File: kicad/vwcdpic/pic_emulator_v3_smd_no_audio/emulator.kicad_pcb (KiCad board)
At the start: 2 copper layers, 24.1 x 18.4 mm, 12 parts, among them P1 CONN_01X05, P2 CONN_01X02, U1 PIC12F629, U2 78L05

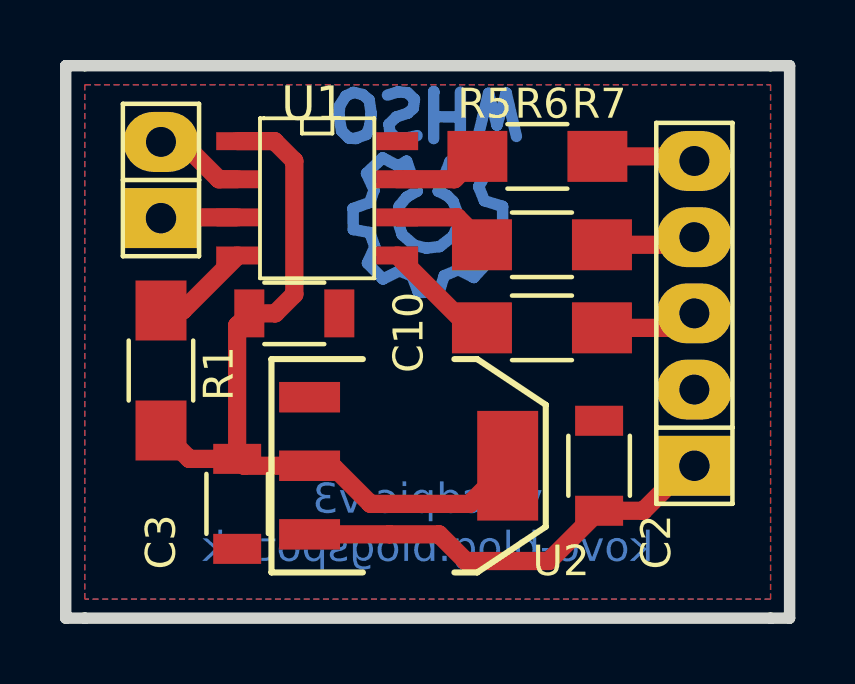
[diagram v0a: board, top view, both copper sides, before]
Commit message: update pcb with soic8 handsoldering module
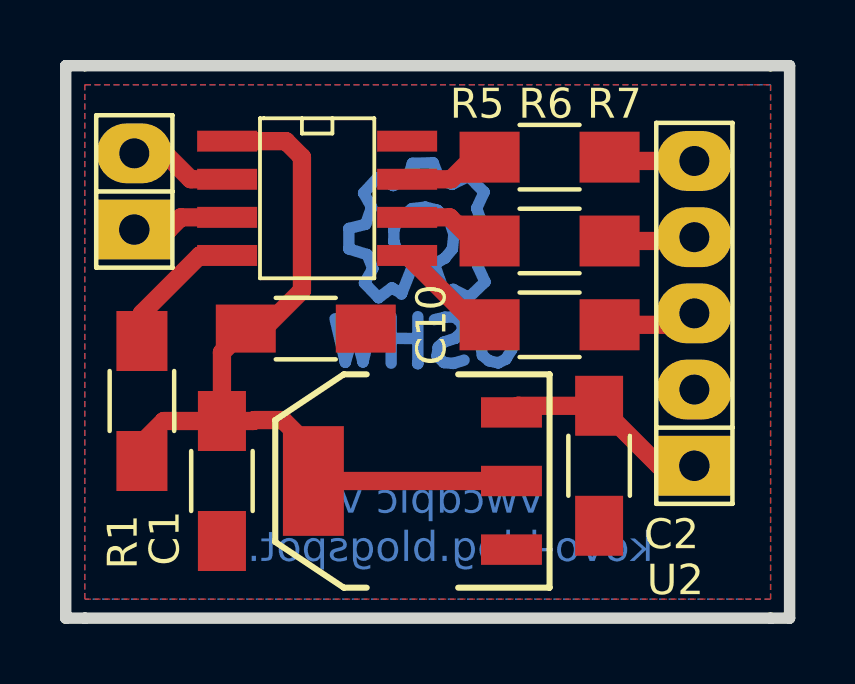
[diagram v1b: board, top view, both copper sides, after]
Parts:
- removed C3: 100n, Capacitors_SMD:C_1206
- added C1: 100n, Capacitors_SMD:C_1206_HandSoldering, F.Cu at (96.0, 58.3)
- C10, C2: footprint Capacitors_SMD:C_1206 -> Capacitors_SMD:C_1206_HandSoldering
- U1: footprint SMD_Packages:SOIC-8-W -> my_modules:SOIC-8-W_long_pads
- moved R1 1.20 mm to (93.3, 55.6)
- moved P2 0.97 mm to (93.1, 48.6)
- moved SYM 0.65 mm to (102.7, 50.2), turned to 180 degrees
- moved C10 0.64 mm to (98.8, 53.2)
- moved U2 0.52 mm to (102.4, 58.3), turned to 90 degrees
- moved R5 0.41 mm to (106.9, 47.5)
- moved R6 0.28 mm to (106.9, 50.3)
- moved R7 0.27 mm to (106.9, 53.1)
- turned C2 to 270 degrees
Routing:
- net POWER_CTL: track 14.6 -> 7.02 mm
- net +5V: track 26.5 -> 27.6 mm
- net Net-(R1-Pad1): track 3.86 -> 4.86 mm
- net Net-(P2-Pad2): track 3.06 -> 4.06 mm
- net Net-(P2-Pad1): track 2.55 -> 3.26 mm
- net DataOut: track 3.08 -> 3.67 mm

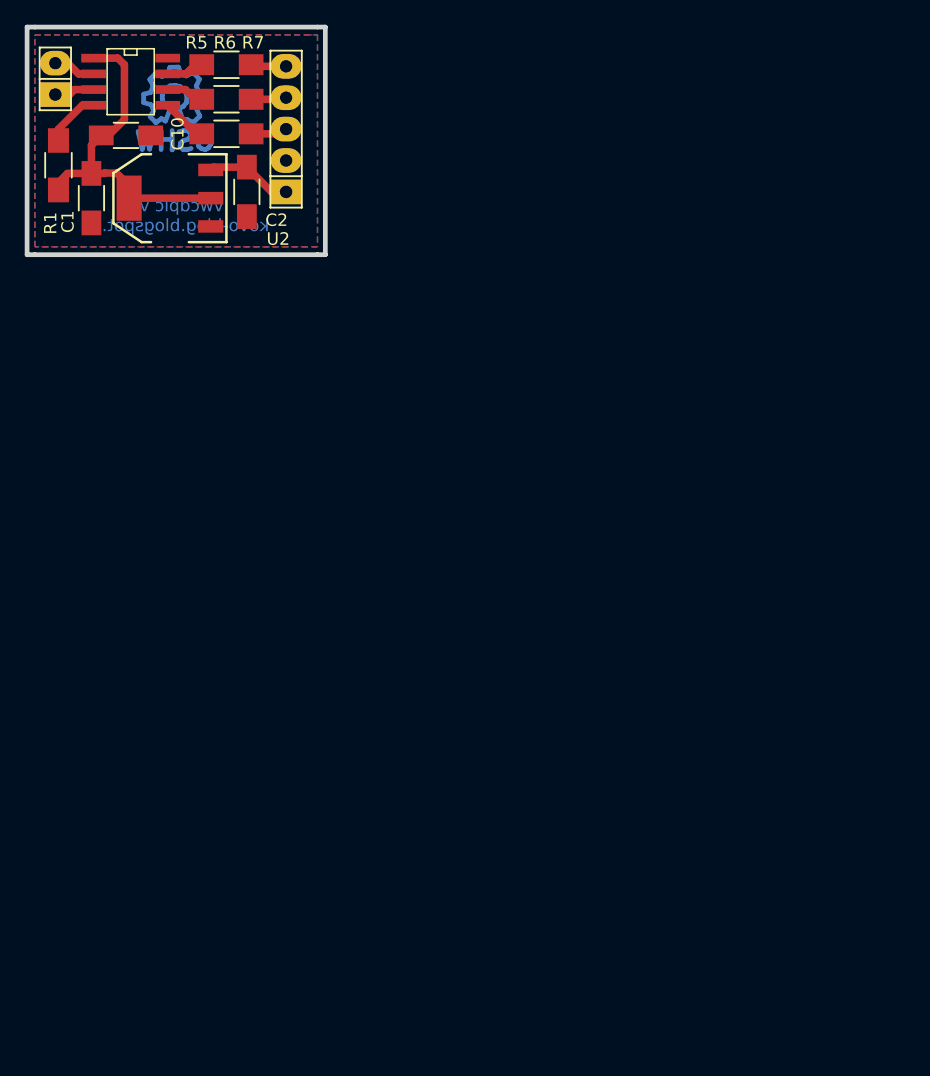
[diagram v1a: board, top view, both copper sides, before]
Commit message: vwcdpic v3 board/panelize
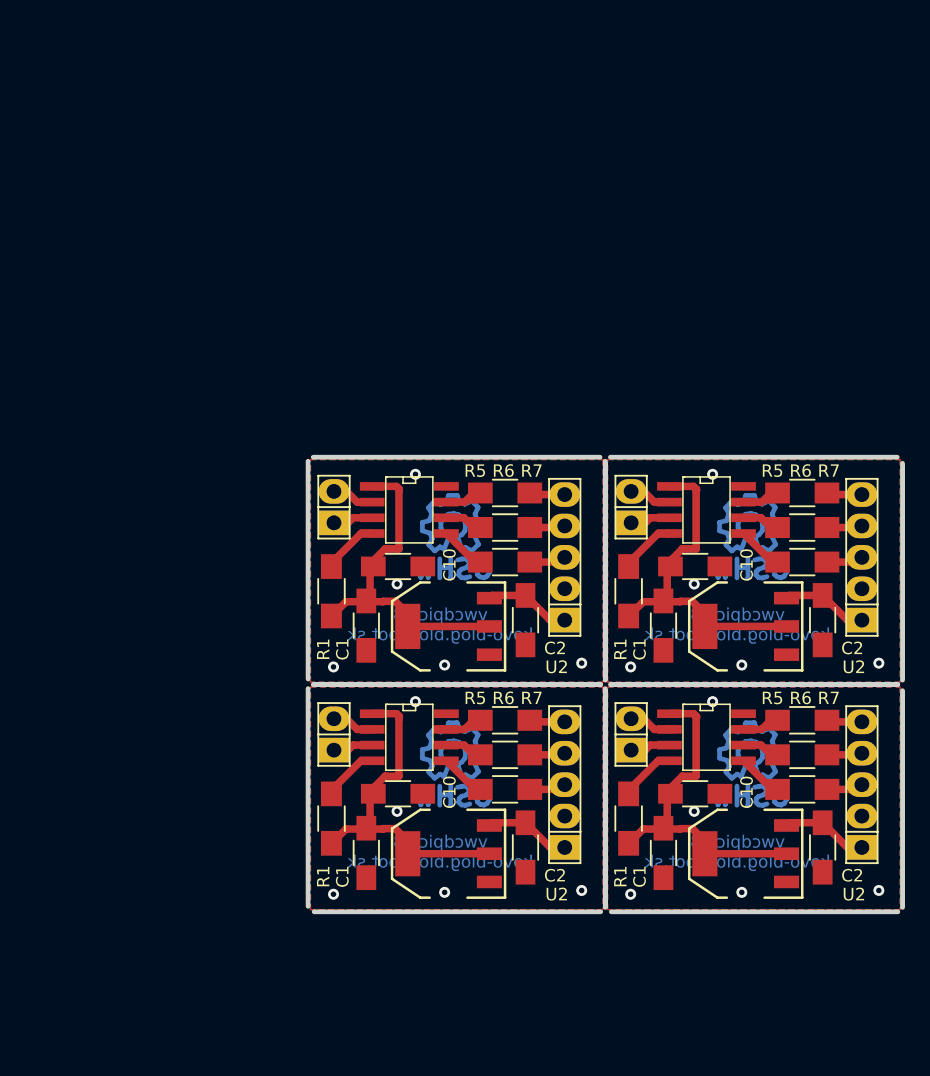
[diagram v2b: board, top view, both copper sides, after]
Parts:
- removed the C1 at (96.0, 58.3)
- removed the C10 at (98.8, 53.2)
- removed the C2 at (108.6, 57.8)
- removed the P1 at (111.8, 52.7)
- removed the P2 at (93.1, 48.6)
- removed the R1 at (93.3, 55.6)
- removed the R5 at (106.9, 47.5)
- removed the R6 at (106.9, 50.3)
- removed the R7 at (106.9, 53.1)
- removed the SYM at (102.7, 50.2)
- removed the U1 at (99.2, 48.9)
- removed the U2 at (102.4, 58.3)
- added C1: 100n, Capacitors_SMD:C_1206_HandSoldering, F.Cu at (118.2, 111.3)
- added C1: 100n, Capacitors_SMD:C_1206_HandSoldering, F.Cu at (118.2, 92.9)
- added C1: 100n, Capacitors_SMD:C_1206_HandSoldering, F.Cu at (142.3, 92.9)
- added C1: 100n, Capacitors_SMD:C_1206_HandSoldering, F.Cu at (142.3, 111.3)
- added C10: 100n, Capacitors_SMD:C_1206_HandSoldering, F.Cu at (120.8, 106.5)
- added C10: 100n, Capacitors_SMD:C_1206_HandSoldering, F.Cu at (120.8, 88.1)
- added C10: 100n, Capacitors_SMD:C_1206_HandSoldering, F.Cu at (144.9, 88.1)
- added C10: 100n, Capacitors_SMD:C_1206_HandSoldering, F.Cu at (144.9, 106.5)
- added C2: 100n, Capacitors_SMD:C_1206_HandSoldering, F.Cu at (131.1, 110.8)
- added C2: 100n, Capacitors_SMD:C_1206_HandSoldering, F.Cu at (131.1, 92.4)
- added C2: 100n, Capacitors_SMD:C_1206_HandSoldering, F.Cu at (155.2, 92.4)
- added C2: 100n, Capacitors_SMD:C_1206_HandSoldering, F.Cu at (155.2, 110.8)
- added P1: CONN_01X05, Pin_Headers:Pin_Header_Straight_1x05, F.Cu at (134.3, 105.7)
- added P1: CONN_01X05, Pin_Headers:Pin_Header_Straight_1x05, F.Cu at (134.3, 87.4)
- added P1: CONN_01X05, Pin_Headers:Pin_Header_Straight_1x05, F.Cu at (158.3, 87.4)
- added P1: CONN_01X05, Pin_Headers:Pin_Header_Straight_1x05, F.Cu at (158.3, 105.7)
- added P2: CONN_01X02, Pin_Headers:Pin_Header_Straight_1x02, F.Cu at (115.6, 101.7)
- added P2: CONN_01X02, Pin_Headers:Pin_Header_Straight_1x02, F.Cu at (115.6, 83.3)
- added P2: CONN_01X02, Pin_Headers:Pin_Header_Straight_1x02, F.Cu at (139.7, 83.3)
- added P2: CONN_01X02, Pin_Headers:Pin_Header_Straight_1x02, F.Cu at (139.7, 101.7)
- added R1: 10k, Resistors_SMD:R_1206_HandSoldering, F.Cu at (115.4, 108.5)
- added R1: 10k, Resistors_SMD:R_1206_HandSoldering, F.Cu at (115.4, 90.1)
- added R1: 10k, Resistors_SMD:R_1206_HandSoldering, F.Cu at (139.5, 90.1)
- added R1: 10k, Resistors_SMD:R_1206_HandSoldering, F.Cu at (139.5, 108.5)
- added R5: 3k3, Resistors_SMD:R_1206_HandSoldering, F.Cu at (129.5, 100.5)
- added R5: 3k3, Resistors_SMD:R_1206_HandSoldering, F.Cu at (129.5, 82.1)
- added R5: 3k3, Resistors_SMD:R_1206_HandSoldering, F.Cu at (153.5, 82.1)
- added R5: 3k3, Resistors_SMD:R_1206_HandSoldering, F.Cu at (153.5, 100.5)
- added R6: 3k3, Resistors_SMD:R_1206_HandSoldering, F.Cu at (129.5, 103.3)
- added R6: 3k3, Resistors_SMD:R_1206_HandSoldering, F.Cu at (129.5, 84.9)
- added R6: 3k3, Resistors_SMD:R_1206_HandSoldering, F.Cu at (153.5, 84.9)
- added R6: 3k3, Resistors_SMD:R_1206_HandSoldering, F.Cu at (153.5, 103.3)
- added R7: 3k3, Resistors_SMD:R_1206_HandSoldering, F.Cu at (129.5, 106.1)
- added R7: 3k3, Resistors_SMD:R_1206_HandSoldering, F.Cu at (129.5, 87.7)
- added R7: 3k3, Resistors_SMD:R_1206_HandSoldering, F.Cu at (153.5, 87.7)
- added R7: 3k3, Resistors_SMD:R_1206_HandSoldering, F.Cu at (153.5, 106.1)
- added SYM: Symbol_OSHW-Logo_CopperTop_07Jul2012, Symbols:Symbol_OSHW-Logo_CopperTop, B.Cu at (125.3, 103.2)
- added SYM: Symbol_OSHW-Logo_CopperTop_07Jul2012, Symbols:Symbol_OSHW-Logo_CopperTop, B.Cu at (125.3, 84.8)
- added SYM: Symbol_OSHW-Logo_CopperTop_07Jul2012, Symbols:Symbol_OSHW-Logo_CopperTop, B.Cu at (149.3, 84.8)
- added SYM: Symbol_OSHW-Logo_CopperTop_07Jul2012, Symbols:Symbol_OSHW-Logo_CopperTop, B.Cu at (149.3, 103.2)
- added U1: PIC12F629, my_modules:SOIC-8-W_long_pads, F.Cu at (121.7, 101.9)
- added U1: PIC12F629, my_modules:SOIC-8-W_long_pads, F.Cu at (121.7, 83.5)
- added U1: PIC12F629, my_modules:SOIC-8-W_long_pads, F.Cu at (145.8, 83.5)
- added U1: PIC12F629, my_modules:SOIC-8-W_long_pads, F.Cu at (145.8, 101.9)
- added U2: 78L05, my_modules:SOT-223-REGULATOR, F.Cu at (124.9, 111.3)
- added U2: 78L05, my_modules:SOT-223-REGULATOR, F.Cu at (124.9, 92.9)
- added U2: 78L05, my_modules:SOT-223-REGULATOR, F.Cu at (148.9, 92.9)
- added U2: 78L05, my_modules:SOT-223-REGULATOR, F.Cu at (148.9, 111.3)
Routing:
- net +5V: track 27.6 -> 113.8 mm
- net POWER_CTL: track 7.02 -> 28.1 mm
- net Net-(R1-Pad1): track 4.86 -> 19.5 mm
- net Net-(R7-Pad1): track 4.12 -> 16.5 mm
- net Net-(P2-Pad2): track 4.06 -> 16.3 mm
- net DataOut: track 3.67 -> 14.7 mm
- net Net-(P2-Pad1): track 3.26 -> 13.1 mm
- net DataIn: track 3.24 -> 13.0 mm
- net Net-(R6-Pad1): track 3.17 -> 12.7 mm
- net CLK: track 3.09 -> 12.4 mm
- net Net-(R5-Pad1): track 3.05 -> 12.2 mm
- net (no net): vias 0 -> 20
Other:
- board size 24.1 x 18.4 mm -> 48.1 x 36.8 mm

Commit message: ..
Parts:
- removed C1 (x4): 100n, Capacitors_SMD:C_1206_HandSoldering
- removed the C10 at (120.8, 106.5)
- removed the C10 at (120.8, 88.1)
- removed the C10 at (144.9, 88.1)
- removed the C10 at (144.9, 106.5)
- removed the C2 at (131.1, 110.8)
- removed the C2 at (131.1, 92.4)
- removed the C2 at (155.2, 92.4)
- removed the C2 at (155.2, 110.8)
- removed the P1 at (134.3, 105.7)
- removed the P1 at (134.3, 87.4)
- removed the P1 at (158.3, 87.4)
- removed the P1 at (158.3, 105.7)
- removed the P2 at (115.6, 101.7)
- removed the P2 at (115.6, 83.3)
- removed the P2 at (139.7, 83.3)
- removed the P2 at (139.7, 101.7)
- removed the R1 at (115.4, 108.5)
- removed the R1 at (115.4, 90.1)
- removed the R1 at (139.5, 90.1)
- removed the R1 at (139.5, 108.5)
- removed the R5 at (129.5, 100.5)
- removed the R5 at (129.5, 82.1)
- removed the R5 at (153.5, 82.1)
- removed the R5 at (153.5, 100.5)
- removed the R6 at (129.5, 103.3)
- removed the R6 at (129.5, 84.9)
- removed the R6 at (153.5, 84.9)
- removed the R6 at (153.5, 103.3)
- removed the R7 at (129.5, 106.1)
- removed the R7 at (129.5, 87.7)
- removed the R7 at (153.5, 87.7)
- removed the R7 at (153.5, 106.1)
- removed SYM (x4): Symbol_OSHW-Logo_CopperTop_07Jul2012, Symbols:Symbol_OSHW-Logo_CopperTop
- removed the U1 at (121.7, 101.9)
- removed the U1 at (121.7, 83.5)
- removed the U1 at (145.8, 83.5)
- removed the U1 at (145.8, 101.9)
- removed the U2 at (124.9, 111.3)
- removed the U2 at (124.9, 92.9)
- removed the U2 at (148.9, 92.9)
- removed the U2 at (148.9, 111.3)
- added C10: 100n, Capacitors_SMD:C_1206_HandSoldering, B.Cu at (147.6, 115.9)
- added C2: 100n, Capacitors_SMD:C_1206_HandSoldering, F.Cu at (138.3, 122.9)
- added P1: CONN_01X05, Pin_Headers:Pin_Header_Straight_1x05, F.Cu at (150.4, 118.9)
- added P2: CONN_01X02, Pin_Headers:Pin_Header_Straight_1x02, F.Cu at (139.5, 116.1)
- added R1: 10k, Resistors_SMD:R_1206_HandSoldering, B.Cu at (147.6, 122.6)
- added R5: 3k3, Resistors_SMD:R_1206_HandSoldering, F.Cu at (145.5, 113.7)
- added R6: 3k3, Resistors_SMD:R_1206_HandSoldering, F.Cu at (145.6, 116.1)
- added R7: 3k3, Resistors_SMD:R_1206_HandSoldering, F.Cu at (145.6, 118.9)
- added U1: PIC12F629, my_modules:SOIC-8-W_long_pads, B.Cu at (143.9, 120.3)
- added U2: 78L05, my_modules:SOT-223-REGULATOR, F.Cu at (144.3, 123.6)
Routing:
- net +5V: track 113.8 -> 18.3 mm, vias 0 -> 1
- net GND: track 0.00 -> 22.5 mm, vias 0 -> 2
- net POWER_CTL: track 28.1 -> 14.9 mm
- net Net-(R1-Pad1): track 19.5 -> 7.81 mm
- net DataOut: track 14.7 -> 4.04 mm
- net DataIn: track 13.0 -> 3.24 mm
- net CLK: track 12.4 -> 3.09 mm
- net Net-(R7-Pad1): track 16.5 -> 8.19 mm, vias 0 -> 1
- net Net-(R6-Pad1): track 12.7 -> 7.00 mm, vias 0 -> 1
- net Net-(P2-Pad1): track 13.1 -> 8.76 mm
- net Net-(R5-Pad1): track 12.2 -> 8.34 mm, vias 0 -> 1
- net Net-(P2-Pad2): track 16.3 -> 13.1 mm, vias 0 -> 1
- net (no net): vias 20 -> 0
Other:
- board outline removed
- net class Default: clearance 0.254 -> 0.1
- net class GND: clearance 0.254 -> 0.1
- rule trace_clearance: 0.254 -> 0.1
- board text removed: "vwcdpic v3 kovo-blog.blogspot.sk"
